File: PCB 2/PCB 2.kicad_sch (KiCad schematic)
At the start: 10 parts, among them M1 Pengda Technology (Fan), U1 LM317L_SOT-89, U2 MCP73831T-2ACI_OT

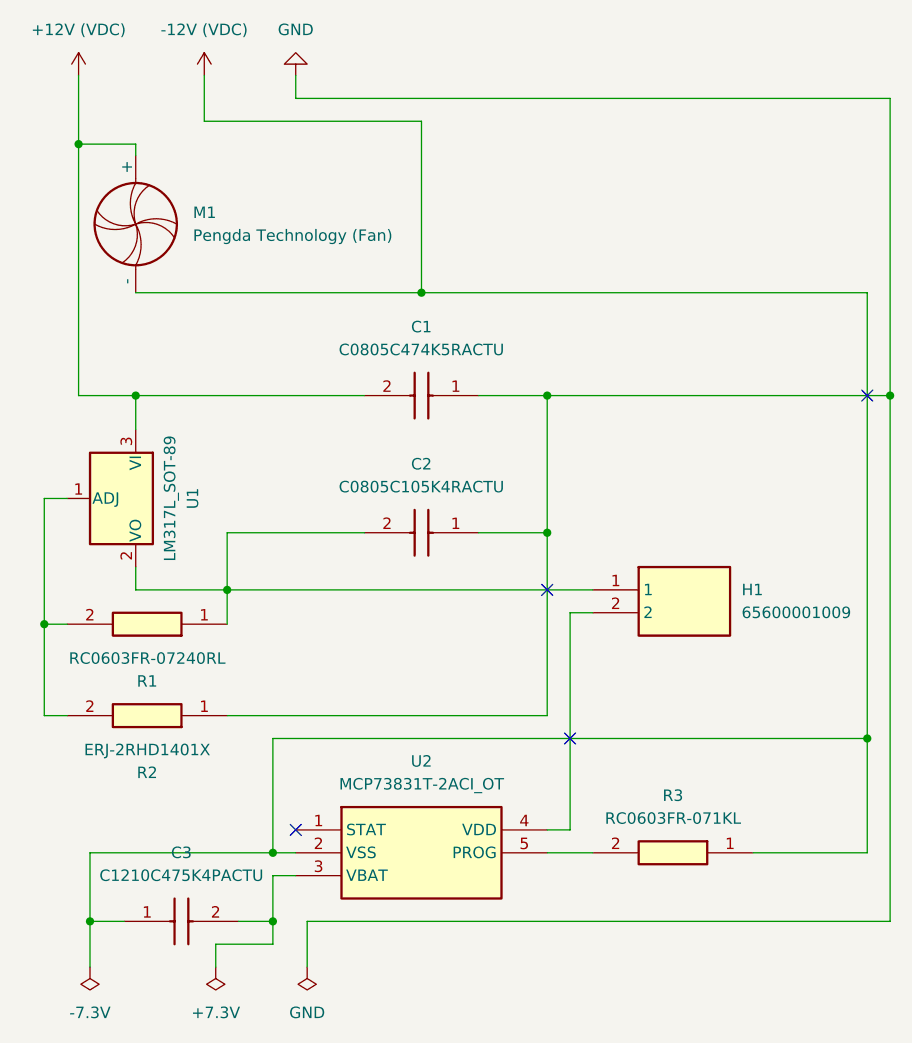
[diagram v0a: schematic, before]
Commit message: Added Output Pins
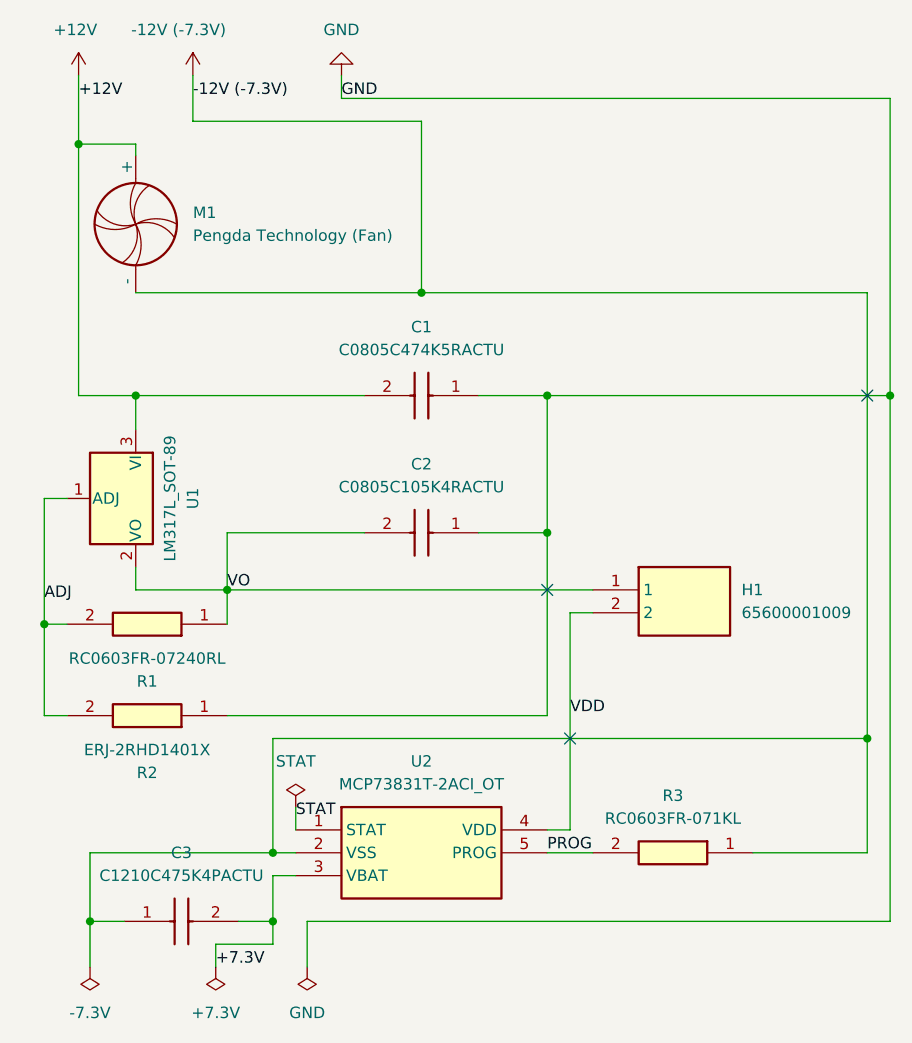
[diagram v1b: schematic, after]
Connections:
- net ADJ: now reaches R1.2, R2.2, U1.1 (ADJ)
- net PROG: now reaches R3.2, U2.5 (PROG)
- net +7.3V: now reaches C3.2, U2.3 (VBAT)
- net VO: now reaches C2.2, H1.1, R1.1, U1.2 (VO)
- net VDD: now reaches H1.2, U2.4 (VDD)
- net STAT: now reaches U2.1 (STAT)
- net +12V (VDC) renamed +12V
- net -12V (VDC) renamed -12V (-7.3V)
- no-connect marks 4 -> 3
